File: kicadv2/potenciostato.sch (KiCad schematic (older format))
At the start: 30 parts, among them J10 test_GND, J11 test_GND, J12 test_GND, J3 Conn_01x03_Male, J4 test_I, J5 test_V, J6 test_DAC, U1 OP77, U2 TL082, U3 OP77, U4 OP77, U5 4316, U6 L7805, U8 L7905

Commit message: hecho esquematico en base a simulacion
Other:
- moved on the sheet: J6, R2, R4
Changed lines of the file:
@@
 NoConn ~ 4950 7850
 Wire Wire Line
-	4050 2750 4600 2750
+	4050 2750 4550 2750
 Wire Wire Line
 	4550 3900 4050 3900
@@
 	5900 4000 6000 4000
 Wire Wire Line
-	6000 2750 6200 2750
+	5750 2750 6200 2750
 Wire Wire Line
 	6000 4000 6000 4350
@@
 L potenciostato-rescue:Conn_01x01_Female-Connector J6
 U 1 1 61851D11
-P 4600 2550
-F 0 "J6" V 4538 2462 50  0000 R CNN
-F 1 "test_DAC" V 4447 2462 50  0000 R CNN
-F 2 "Connector_PinHeader_1.00mm:PinHeader_1x01_P1.00mm_Vertical" H 4600 2550 50  0001 C CNN
-F 3 "~" H 4600 2550 50  0001 C CNN
-	1    4600 2550
+P 4550 2550
+F 0 "J6" V 4488 2462 50  0000 R CNN
+F 1 "test_DAC" V 4397 2462 50  0000 R CNN
+F 2 "Connector_PinHeader_1.00mm:PinHeader_1x01_P1.00mm_Vertical" H 4550 2550 50  0001 C CNN
+F 3 "~" H 4550 2550 50  0001 C CNN
+	1    4550 2550
 	0    -1   -1   0
 $EndComp
@@
 L potenciostato-rescue:R-Device R2
 U 1 1 5CC25964
-P 5850 2750
-F 0 "R2" V 5643 2750 50  0000 C CNN
-F 1 "100K" V 5734 2750 50  0000 C CNN
-F 2 "Resistor_SMD:R_1206_3216Metric_Pad1.30x1.75mm_HandSolder" V 5780 2750 50  0001 C CNN
-F 3 "~" H 5850 2750 50  0001 C CNN
-	1    5850 2750
+P 5600 2750
+F 0 "R2" V 5393 2750 50  0000 C CNN
+F 1 "100K" V 5484 2750 50  0000 C CNN
+F 2 "Resistor_SMD:R_1206_3216Metric_Pad1.30x1.75mm_HandSolder" V 5530 2750 50  0001 C CNN
+F 3 "~" H 5600 2750 50  0001 C CNN
+	1    5600 2750
 	0    1    1    0
 $EndComp
@@
 L potenciostato-rescue:R-Device R4
 U 1 1 5F9FD20A
-P 6400 5250
-F 0 "R4" V 6193 5250 50  0000 C CNN
-F 1 "10K" V 6284 5250 50  0000 C CNN
-F 2 "Resistor_SMD:R_1206_3216Metric_Pad1.30x1.75mm_HandSolder" V 6330 5250 50  0001 C CNN
-F 3 "~" H 6400 5250 50  0001 C CNN
-	1    6400 5250
+P 6500 5250
+F 0 "R4" V 6293 5250 50  0000 C CNN
+F 1 "10K" V 6384 5250 50  0000 C CNN
+F 2 "Resistor_SMD:R_1206_3216Metric_Pad1.30x1.75mm_HandSolder" V 6430 5250 50  0001 C CNN
+F 3 "~" H 6500 5250 50  0001 C CNN
+	1    6500 5250
 	0    1    1    0
 $EndComp
@@
 	2650 3950 3050 3950
 Wire Wire Line
-	6250 5250 6150 5250
+	6350 5250 6150 5250
 Wire Wire Line
 	6150 5250 6150 6800
@@
 F0 "salida_dac" 50
 F1 "salida_dac.sch" 50
-F2 "VIN" I R 4050 2750 50
+F2 "VIN" O R 4050 2750 50
 F3 "I_IN" I L 3050 3700 50
 F4 "V_IN" I R 4050 3900 50
-F5 "gan_x1" I L 3050 4250 50
-F6 "gan_x5" I L 3050 4100 50
-F7 "gan_x0.1" I L 3050 4400 50
-F8 "gan_x10" I L 3050 3950 50
+F5 "gan_x1" O L 3050 4250 50
+F6 "gan_x5" O L 3050 4100 50
+F7 "gan_x0.1" O L 3050 4400 50
+F8 "gan_x10" O L 3050 3950 50
 $EndSheet
 Wire Wire Line
@@
 	0    -1   -1   0
 $EndComp
-Wire Wire Line
-	6550 5250 6850 5250
 Wire Wire Line
 	7700 4600 8200 4600
@@
 	900  4650 1250 4650
 Connection ~ 1250 4650
-Connection ~ 4600 2750
-Wire Wire Line
-	4600 2750 5700 2750
 $Comp
 L Device:D_Bridge_+-AA D?
@@
 Wire Wire Line
 	1550 1650 1900 1650
+Wire Wire Line
+	6650 5250 6850 5250
+Connection ~ 4550 2750
+Wire Wire Line
+	4550 2750 5450 2750
 $EndSCHEMATC

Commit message: trazando pcb
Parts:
- added J13: AC2, Connector_PinHeader_1.00mm:PinHeader_1x01_P1.00mm_Vertical, symbol potenciostato-rescue:Conn_01x01_Female-Connector
- added J9: AC1, Connector_PinHeader_1.00mm:PinHeader_1x01_P1.00mm_Vertical, symbol potenciostato-rescue:Conn_01x01_Female-Connector
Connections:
- net at TR1.1: now also J13.1 (Pin_1)
- net at TR1.3: now also J9.1 (Pin_1)
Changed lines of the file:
@@
 Wire Wire Line
 	4550 2750 5450 2750
+$Comp
+L potenciostato-rescue:Conn_01x01_Female-Connector J13
+U 1 1 63685931
+P 950 1650
+F 0 "J13" H 888 1562 50  0000 R CNN
+F 1 "AC2" H 1100 1450 50  0000 R CNN
+F 2 "Connector_PinHeader_1.00mm:PinHeader_1x01_P1.00mm_Vertical" H 950 1650 50  0001 C CNN
+F 3 "~" H 950 1650 50  0001 C CNN
+	1    950  1650
+	-1   0    0    1
+$EndComp
+$Comp
+L potenciostato-rescue:Conn_01x01_Female-Connector J9
+U 1 1 636995B8
+P 950 1250
+F 0 "J9" H 888 1162 50  0000 R CNN
+F 1 "AC1" H 1100 1050 50  0000 R CNN
+F 2 "Connector_PinHeader_1.00mm:PinHeader_1x01_P1.00mm_Vertical" H 950 1250 50  0001 C CNN
+F 3 "~" H 950 1250 50  0001 C CNN
+	1    950  1250
+	-1   0    0    1
+$EndComp
 $EndSCHEMATC

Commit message: modificado SCH?
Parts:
- J10, J11, J12, J13, J4, J5, J6, J9: footprint Connector_PinHeader_1.00mm:PinHeader_1x01_P1.00mm_Vertical -> Connector_PinHeader_2.54mm:PinHeader_1x01_P2.54mm_Vertical
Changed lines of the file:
@@
 F 0 "J4" V 2488 3412 50  0000 R CNN
 F 1 "test_I" V 2397 3412 50  0000 R CNN
-F 2 "Connector_PinHeader_1.00mm:PinHeader_1x01_P1.00mm_Vertical" H 2550 3500 50  0001 C CNN
+F 2 "Connector_PinHeader_2.54mm:PinHeader_1x01_P2.54mm_Vertical" H 2550 3500 50  0001 C CNN
 F 3 "~" H 2550 3500 50  0001 C CNN
 	1    2550 3500
@@
 F 0 "J6" V 4488 2462 50  0000 R CNN
 F 1 "test_DAC" V 4397 2462 50  0000 R CNN
-F 2 "Connector_PinHeader_1.00mm:PinHeader_1x01_P1.00mm_Vertical" H 4550 2550 50  0001 C CNN
+F 2 "Connector_PinHeader_2.54mm:PinHeader_1x01_P2.54mm_Vertical" H 4550 2550 50  0001 C CNN
 F 3 "~" H 4550 2550 50  0001 C CNN
 	1    4550 2550
@@
 F 0 "J5" V 4488 3612 50  0000 R CNN
 F 1 "test_V" V 4397 3612 50  0000 R CNN
-F 2 "Connector_PinHeader_1.00mm:PinHeader_1x01_P1.00mm_Vertical" H 4550 3700 50  0001 C CNN
+F 2 "Connector_PinHeader_2.54mm:PinHeader_1x01_P2.54mm_Vertical" H 4550 3700 50  0001 C CNN
 F 3 "~" H 4550 3700 50  0001 C CNN
 	1    4550 3700
@@
 F 0 "J12" H 1538 4362 50  0000 R CNN
 F 1 "test_GND" H 1750 4250 50  0000 R CNN
-F 2 "Connector_PinHeader_1.00mm:PinHeader_1x01_P1.00mm_Vertical" H 1600 4450 50  0001 C CNN
+F 2 "Connector_PinHeader_2.54mm:PinHeader_1x01_P2.54mm_Vertical" H 1600 4450 50  0001 C CNN
 F 3 "~" H 1600 4450 50  0001 C CNN
 	1    1600 4450
@@
 F 0 "J11" H 1188 4362 50  0000 R CNN
 F 1 "test_GND" H 1400 4250 50  0000 R CNN
-F 2 "Connector_PinHeader_1.00mm:PinHeader_1x01_P1.00mm_Vertical" H 1250 4450 50  0001 C CNN
+F 2 "Connector_PinHeader_2.54mm:PinHeader_1x01_P2.54mm_Vertical" H 1250 4450 50  0001 C CNN
 F 3 "~" H 1250 4450 50  0001 C CNN
 	1    1250 4450
@@
 F 0 "J10" H 838 4362 50  0000 R CNN
 F 1 "test_GND" H 1050 4250 50  0000 R CNN
-F 2 "Connector_PinHeader_1.00mm:PinHeader_1x01_P1.00mm_Vertical" H 900 4450 50  0001 C CNN
+F 2 "Connector_PinHeader_2.54mm:PinHeader_1x01_P2.54mm_Vertical" H 900 4450 50  0001 C CNN
 F 3 "~" H 900 4450 50  0001 C CNN
 	1    900  4450
@@
 F 0 "J13" H 888 1562 50  0000 R CNN
 F 1 "AC2" H 1100 1450 50  0000 R CNN
-F 2 "Connector_PinHeader_1.00mm:PinHeader_1x01_P1.00mm_Vertical" H 950 1650 50  0001 C CNN
+F 2 "Connector_PinHeader_2.54mm:PinHeader_1x01_P2.54mm_Vertical" H 950 1650 50  0001 C CNN
 F 3 "~" H 950 1650 50  0001 C CNN
 	1    950  1650
@@
 F 0 "J9" H 888 1162 50  0000 R CNN
 F 1 "AC1" H 1100 1050 50  0000 R CNN
-F 2 "Connector_PinHeader_1.00mm:PinHeader_1x01_P1.00mm_Vertical" H 950 1250 50  0001 C CNN
+F 2 "Connector_PinHeader_2.54mm:PinHeader_1x01_P2.54mm_Vertical" H 950 1250 50  0001 C CNN
 F 3 "~" H 950 1250 50  0001 C CNN
 	1    950  1250

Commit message: puestos USBy trafo OK
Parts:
- TR1: footprint RF_Mini-Circuits:Mini-Circuits_CD637_H5.23mm -> kicadv2:Transformador_7.5V
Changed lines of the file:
@@
 F 0 "TR1" H 1350 1831 50  0000 C CNN
 F 1 "ADT2-71T" H 1350 1740 50  0000 C CNN
-F 2 "RF_Mini-Circuits:Mini-Circuits_CD637_H5.23mm" H 1350 1100 50  0001 C CNN
+F 2 "kicadv2:Transformador_7.5V" H 1350 1100 50  0001 C CNN
 F 3 "https://www.minicircuits.com/pdfs/ADT2-71T+.pdf" H 1350 1450 50  0001 C CNN
 	1    1350 1450

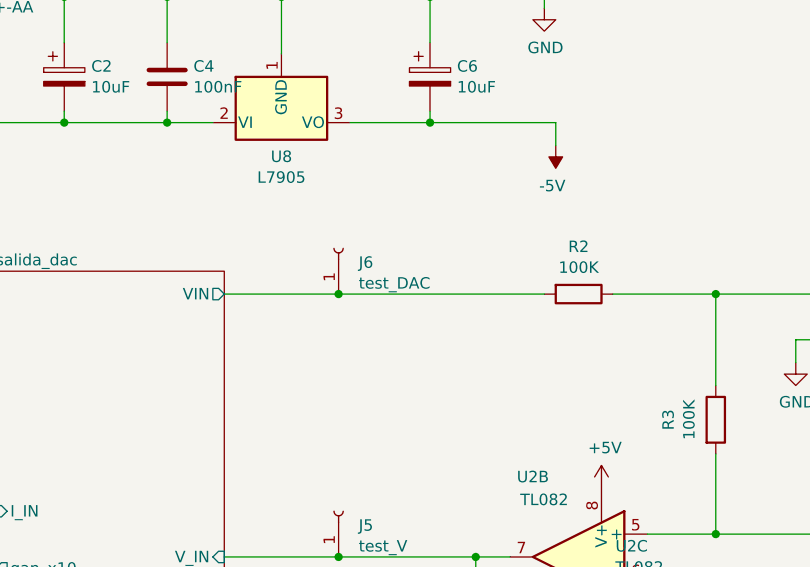
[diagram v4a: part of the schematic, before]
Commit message: modificaciones esteticas en el pcb y test_DAC por test_VIN
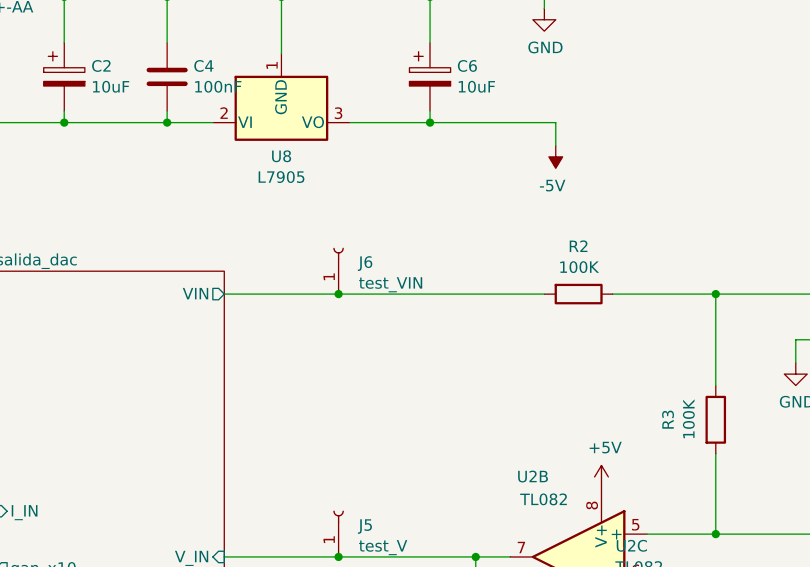
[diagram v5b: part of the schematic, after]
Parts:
- J6: value test_DAC -> test_VIN
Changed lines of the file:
@@
 P 4550 2550
 F 0 "J6" V 4488 2462 50  0000 R CNN
-F 1 "test_DAC" V 4397 2462 50  0000 R CNN
+F 1 "test_VIN" V 4397 2462 50  0000 R CNN
 F 2 "Connector_PinHeader_2.54mm:PinHeader_1x01_P2.54mm_Vertical" H 4550 2550 50  0001 C CNN
 F 3 "~" H 4550 2550 50  0001 C CNN

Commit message: planos de masa, gerber
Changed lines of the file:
@@
 	-1   0    0    1
 $EndComp
+$Comp
+L power:GNDD #PWR0119
+U 1 1 636D1318
+P 5700 1500
+F 0 "#PWR0119" H 5700 1250 50  0001 C CNN
+F 1 "GNDD" H 5704 1345 50  0000 C CNN
+F 2 "" H 5700 1500 50  0001 C CNN
+F 3 "" H 5700 1500 50  0001 C CNN
+	1    5700 1500
+	1    0    0    -1
+$EndComp
+Wire Wire Line
+	5450 1450 5700 1450
+Wire Wire Line
+	5700 1450 5700 1500
+Connection ~ 5450 1450
 $EndSCHEMATC

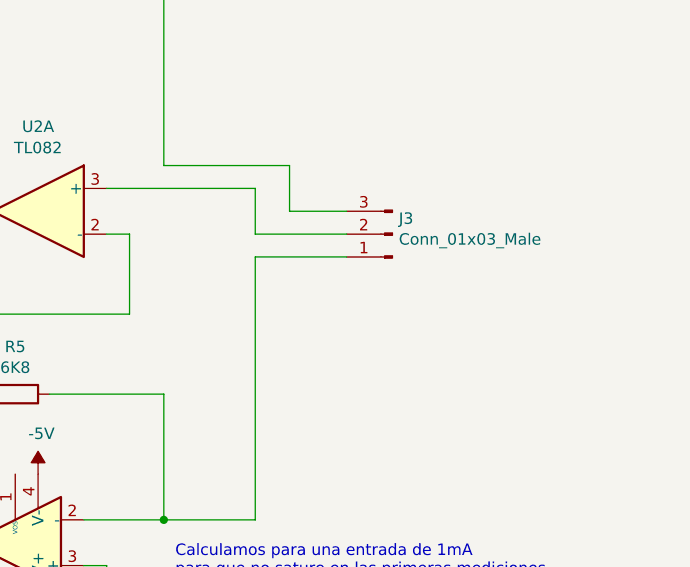
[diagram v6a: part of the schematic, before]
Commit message: agregado logo potencio al b.silk, falta generar gerber y taladro de vuelta
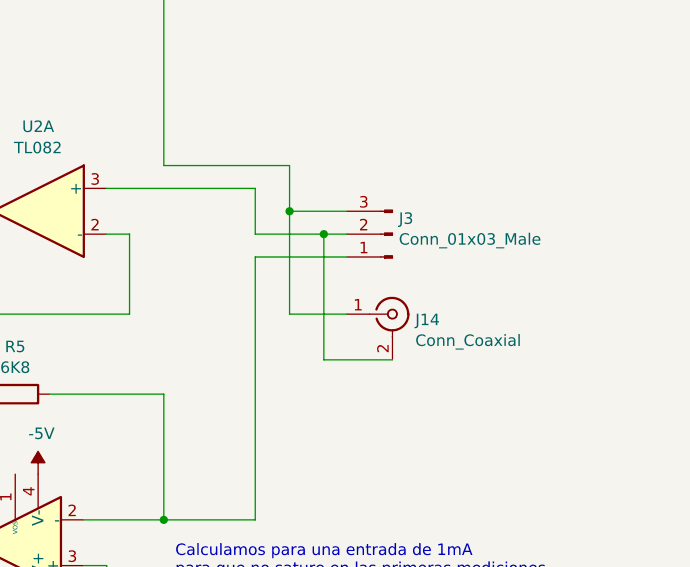
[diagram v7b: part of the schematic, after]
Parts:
- added J14: Conn_Coaxial, Connector_Coaxial:BNC_Amphenol_B6252HB-NPP3G-50_Horizontal, symbol Connector:Conn_Coaxial
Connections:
- net at J3.3 (Pin_3), U3.6: now also J14.1 (In)
- net at J3.2 (Pin_2), U2.3 (+): now also J14.2 (Ext)
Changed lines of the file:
@@
 	8600 3700 8600 3900
 Wire Wire Line
-	8600 3900 9000 3900
+	8600 3900 8900 3900
 Wire Wire Line
 	8600 4000 8600 5150
@@
 	5700 1450 5700 1500
 Connection ~ 5450 1450
+$Comp
+L Connector:Conn_Coaxial J14
+U 1 1 636ED754
+P 9200 4250
+F 0 "J14" H 9300 4225 50  0000 L CNN
+F 1 "Conn_Coaxial" H 9300 4134 50  0000 L CNN
+F 2 "Connector_Coaxial:BNC_Amphenol_B6252HB-NPP3G-50_Horizontal" H 9200 4250 50  0001 C CNN
+F 3 " ~" H 9200 4250 50  0001 C CNN
+	1    9200 4250
+	1    0    0    -1
+$EndComp
+Wire Wire Line
+	9000 4250 8750 4250
+Wire Wire Line
+	8750 4250 8750 3800
+Connection ~ 8750 3800
+Wire Wire Line
+	9200 4450 8900 4450
+Wire Wire Line
+	8900 4450 8900 3900
+Connection ~ 8900 3900
+Wire Wire Line
+	8900 3900 9000 3900
 $EndSCHEMATC
